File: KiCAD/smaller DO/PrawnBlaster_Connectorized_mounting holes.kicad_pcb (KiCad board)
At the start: 2 copper layers, 93 x 58.4 mm, 30 parts, among them IC1 74LVT245D,118, J2 Ext. Clock, J3 Ext. Trig., J4 Pseudoclock 3, J5 Pseudoclock 1, J6 Pseudoclock 2, J7 Pseudoclock 0, U2 74LVC1G34, U3 Pico, U4 74LVC1G17

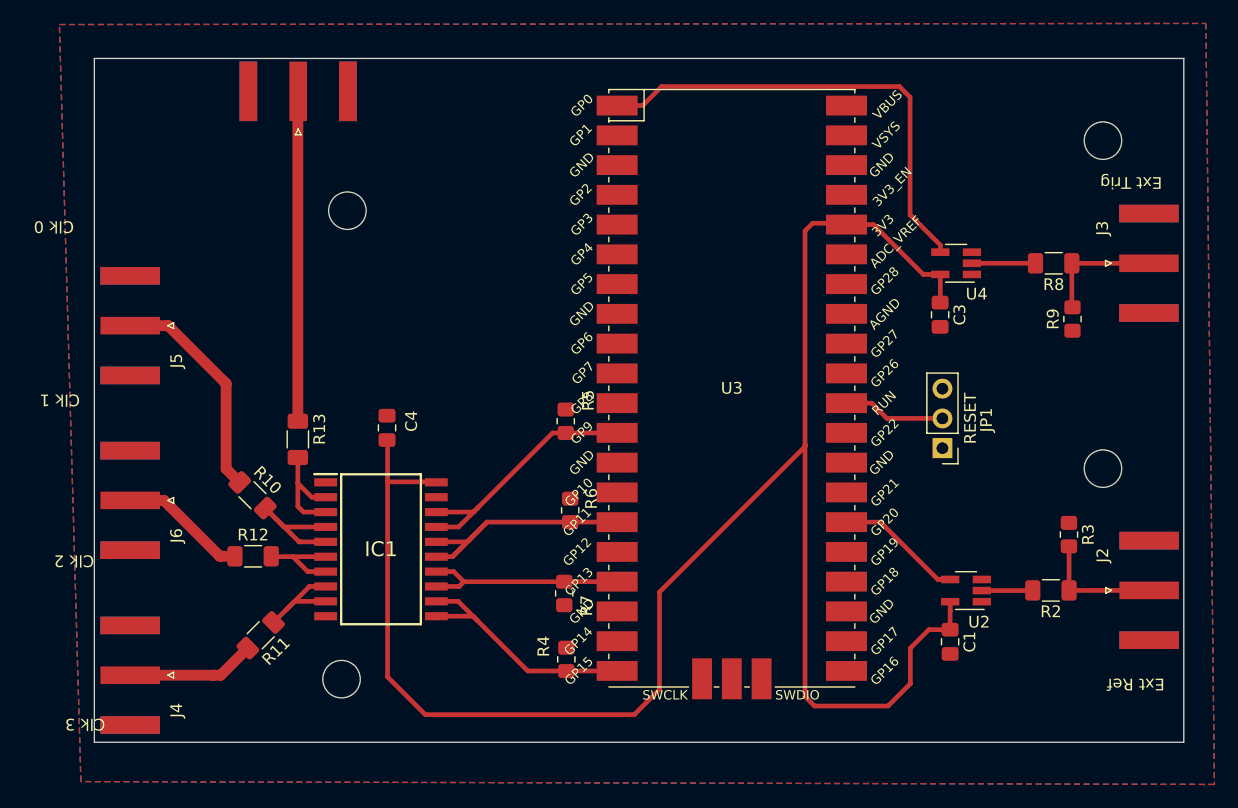
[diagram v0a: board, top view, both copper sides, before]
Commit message: I moved The holes to align with the other board
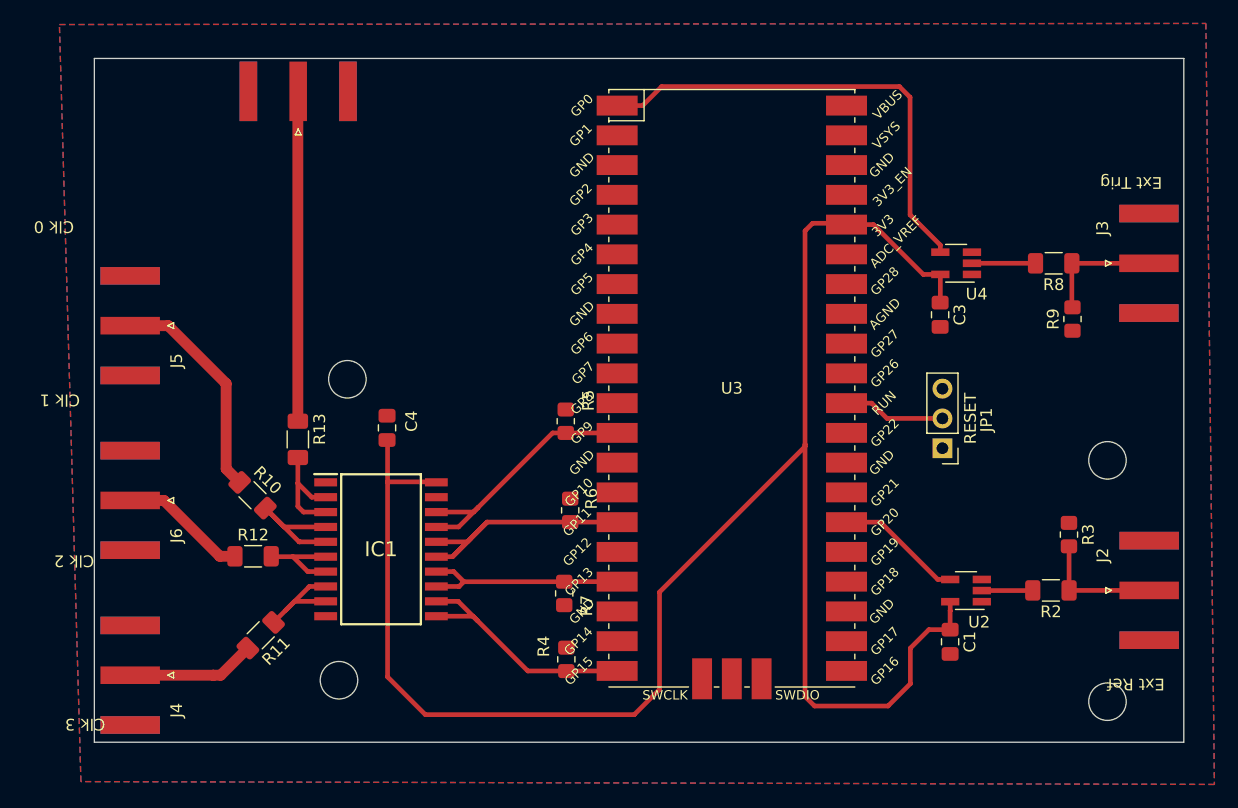
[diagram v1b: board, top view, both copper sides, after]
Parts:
- moved REF** 27.3 mm to (168.2, 100.2)
- moved REF** 19.9 mm to (168.2, 120.8)
- moved REF** 14.4 mm to (103.3, 93.3)
- moved REF** 0.24 mm to (102.6, 119.0)
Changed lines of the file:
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@@
   (net 50 "unconnected-(U3-GPIO21-Pad27)")
   (footprint "MountingHole:MountingHole_3.2mm_M3_ISO7380" (layer "F.Cu")
-    (at 167.7752 72.8624 180)
+    (at 168.1582 100.1544 180)
     (descr "Mounting Hole 3.2mm, no annular, M3, ISO7380")
     (tags "mounting hole 3.2mm no annular m3 iso7380")
@@
   )
   (footprint "MountingHole:MountingHole_3.2mm_M3_ISO7380" (layer "F.Cu")
-    (at 102.7752 118.8624 180)
+    (at 102.5582 118.9544 180)
     (descr "Mounting Hole 3.2mm, no annular, M3, ISO7380")
     (tags "mounting hole 3.2mm no annular m3 iso7380")
@@
   )
   (footprint "MountingHole:MountingHole_3.2mm_M3_ISO7380" (layer "F.Cu")
-    (at 103.2752 78.8624 180)
+    (at 103.2752 93.2544 180)
     (descr "Mounting Hole 3.2mm, no annular, M3, ISO7380")
     (tags "mounting hole 3.2mm no annular m3 iso7380")
@@
   )
   (footprint "MountingHole:MountingHole_3.2mm_M3_ISO7380" (layer "F.Cu")
-    (at 167.7752 100.8624 180)
+    (at 168.1582 120.7544 180)
     (descr "Mounting Hole 3.2mm, no annular, M3, ISO7380")
     (tags "mounting hole 3.2mm no annular m3 iso7380")
@@
     )
   )
-  (gr_rect (start 174.6752 124.2398) (end 81.6752 65.8704)
+  (gr_rect (start 81.6752 65.8704) (end 174.6752 124.2398)
     (stroke (width 0.1) (type solid)) (fill none) (layer "Edge.Cuts"))
   (gr_text "Ext Ref" (at 170.5804 119.2808 180) (layer "F.SilkS")
